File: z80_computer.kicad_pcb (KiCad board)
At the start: 2 copper layers, 15 parts, among them J7 CompactFlash Port, U12 Z84C40-SIO-0, U24 OPEN-SMART-3.5

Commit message: Updating PCB. moving ram to middle, IO to lower part
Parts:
- removed C30: 220u, Capacitor_THT:CP_Radial_D8.0mm_P3.80mm
- removed C33: 100n, Capacitor_THT:C_Disc_D5.0mm_W2.5mm_P2.50mm
- removed H5: PlaceHolder Sea80, z80_computer:wave_logo
- removed H6: PlaceHolder for OS Hardware, Symbol:OSHW-Logo_19x20mm_SilkScreen
- removed H7: Placeholder Graphic, Symbol:Symbol_Barrel_Polarity
- removed J7: CompactFlash Port, Personal:CompactFlash_Module
- removed R30, R31: 10k, Resistor_THT:R_Axial_DIN0207_L6.3mm_D2.5mm_P10.16mm_Horizontal
- removed R6: 1k, Resistor_THT:R_Axial_DIN0207_L6.3mm_D2.5mm_P10.16mm_Horizontal
- removed REF**: Symbol_CC-ShareAlike_CopperTop_Small, Symbol:Symbol_CC-ShareAlike_CopperTop_Small
- removed REF**: Symbol_CC-Noncommercial_CopperTop_Small, Symbol:Symbol_CC-Noncommercial_CopperTop_Small
- removed REF**: Symbol_CC-Attribution_CopperTop_Small, Symbol:Symbol_CC-Attribution_CopperTop_Small
- removed REF**: Symbol_CreativeCommons_CopperTop_Type2_Small, Symbol:Symbol_CreativeCommons_CopperTop_Type2_Small
- removed U12: Z84C40-SIO-0, Package_DIP:DIP-40_W15.24mm_Socket_LongPads

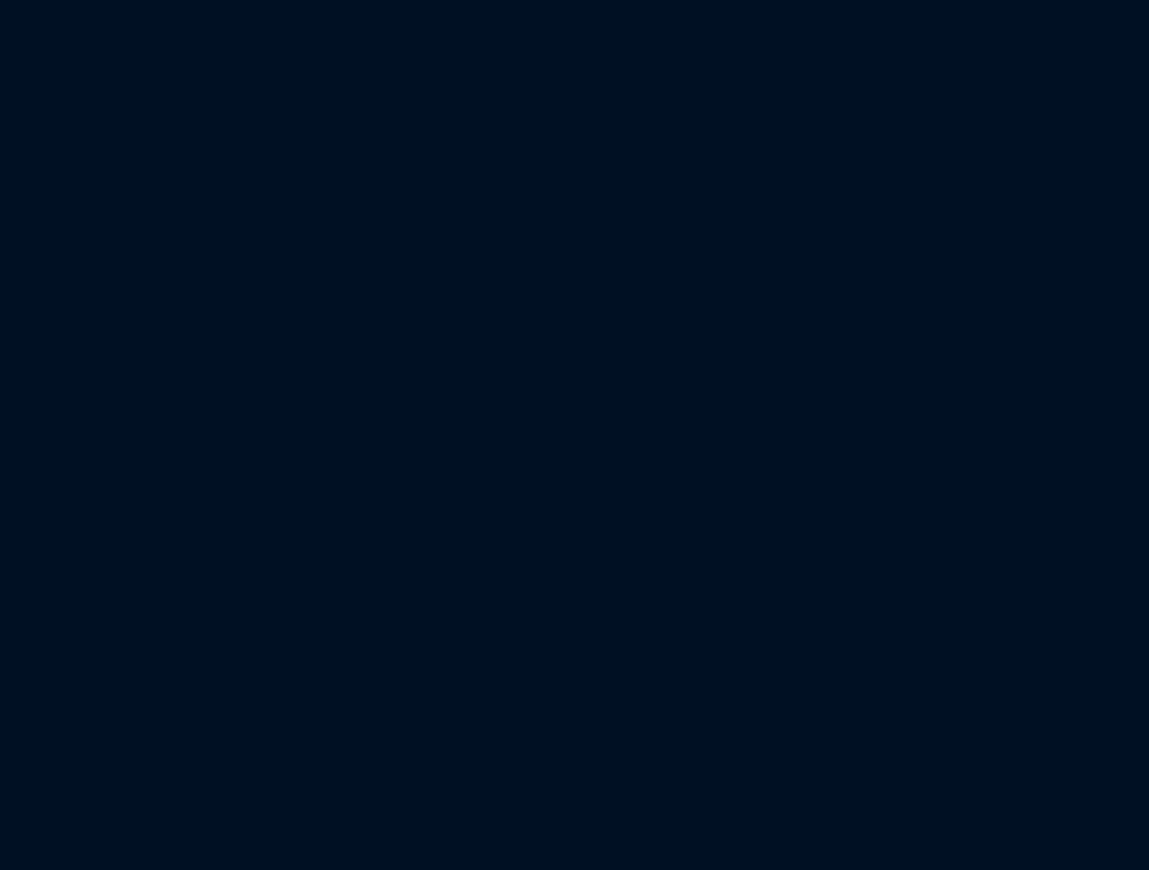
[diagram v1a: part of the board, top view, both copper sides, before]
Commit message: Board rerouted. Missing Creative commons
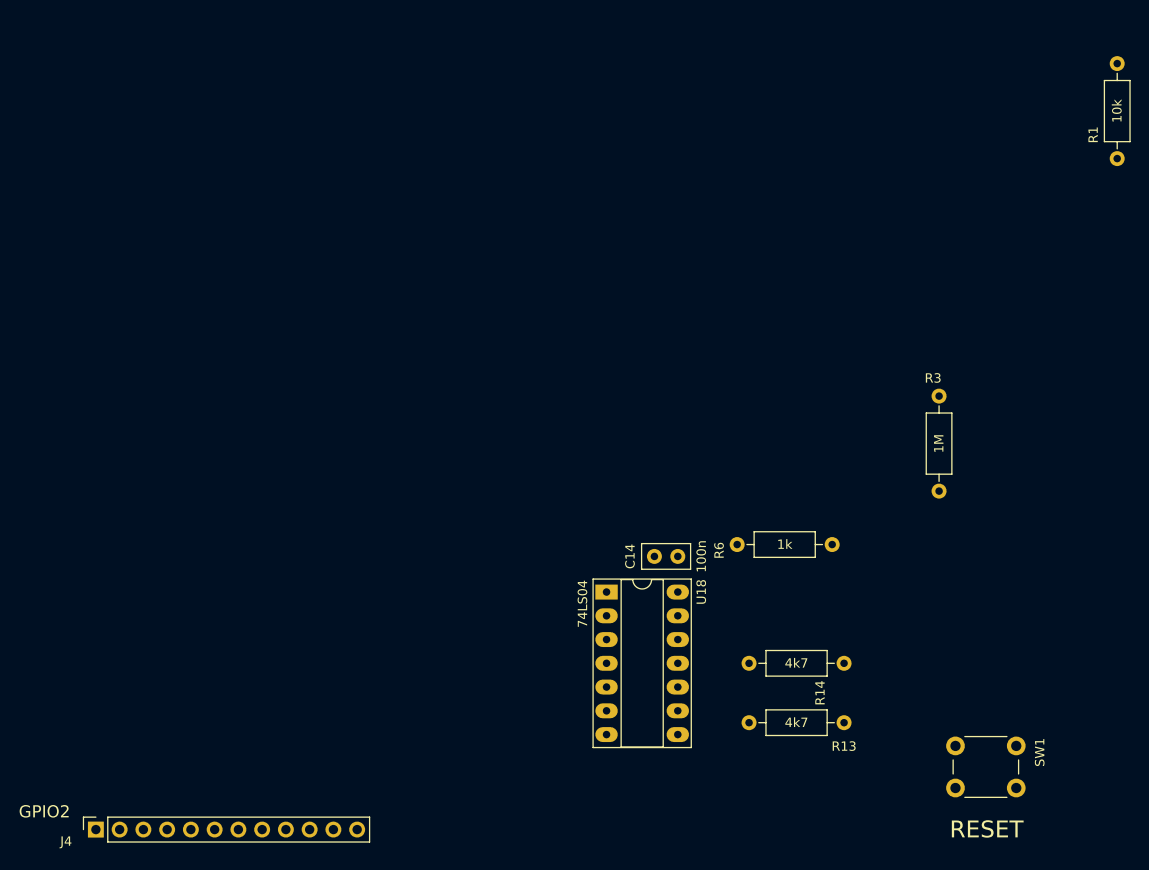
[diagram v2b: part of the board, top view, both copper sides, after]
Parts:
- added C14: 100n, Capacitor_THT:C_Disc_D5.0mm_W2.5mm_P2.50mm, F.Cu at (288.3, 189.2)
- added J4: GPIO2, Connector_PinSocket_2.54mm:PinSocket_1x12_P2.54mm_Vertical, F.Cu at (226.1, 218.4)
- added R1: 10k, Resistor_THT:R_Axial_DIN0207_L6.3mm_D2.5mm_P10.16mm_Horizontal, F.Cu at (335.3, 136.5)
- added R13: 4k7, Resistor_THT:R_Axial_DIN0207_L6.3mm_D2.5mm_P10.16mm_Horizontal, F.Cu at (306.1, 207.0)
- added R14: 4k7, Resistor_THT:R_Axial_DIN0207_L6.3mm_D2.5mm_P10.16mm_Horizontal, F.Cu at (306.1, 200.7)
- added R3: 1M, Resistor_THT:R_Axial_DIN0207_L6.3mm_D2.5mm_P10.16mm_Horizontal, F.Cu at (316.2, 182.2)
- added R6: 1k, Resistor_THT:R_Axial_DIN0207_L6.3mm_D2.5mm_P10.16mm_Horizontal, F.Cu at (294.6, 188.0)
- added SW1: RESET, Button_Switch_THT:SW_PUSH_6mm, F.Cu at (324.5, 214.0)
- added U18: 74LS04, Package_DIP:DIP-14_W7.62mm_Socket_LongPads, F.Cu at (280.7, 193.0)
